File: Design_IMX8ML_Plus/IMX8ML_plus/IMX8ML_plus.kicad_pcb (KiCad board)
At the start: 6 copper layers, 50 x 80 mm, 167 parts, among them J1 DF40C-100DP-0.4V_51_, J2 DF40C-100DP-0.4V_51_, J3 DF40C-100DP-0.4V_51_, J4 DF40C-100DP-0.4V_51_, U1 MIMX8ML8CVNKZAB, U2 MT53E1536M32D4DT-046 WT:A, U3 SDINBDG4-8G, U4 PCA9450CHNY, U5 MT25QUxxxxxx1xW7, U6 KSZ9131RNXI, Y1 32.768KHz, Y2 24MHz, Y3 32.768KHz

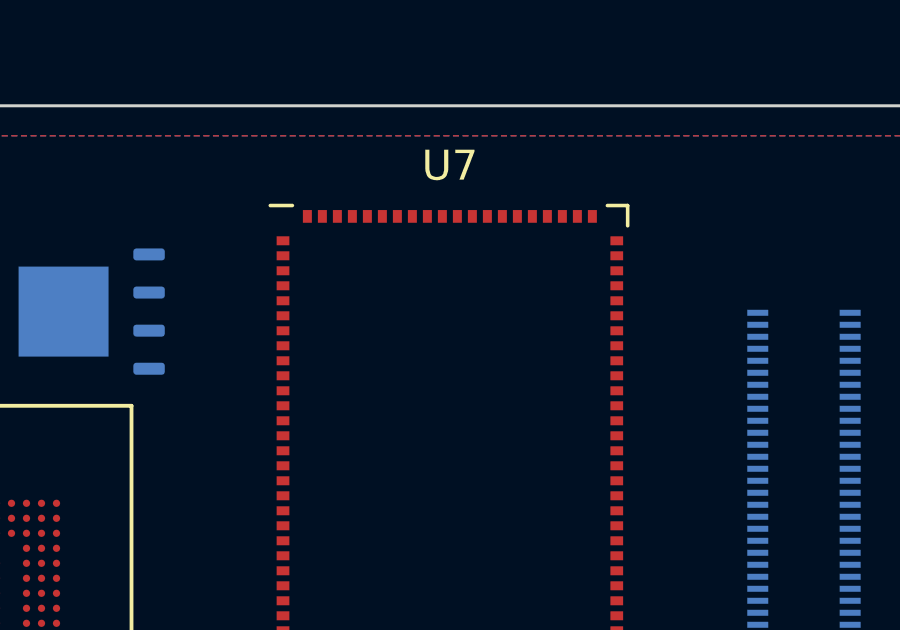
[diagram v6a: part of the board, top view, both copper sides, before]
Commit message: reorganization of the componentes
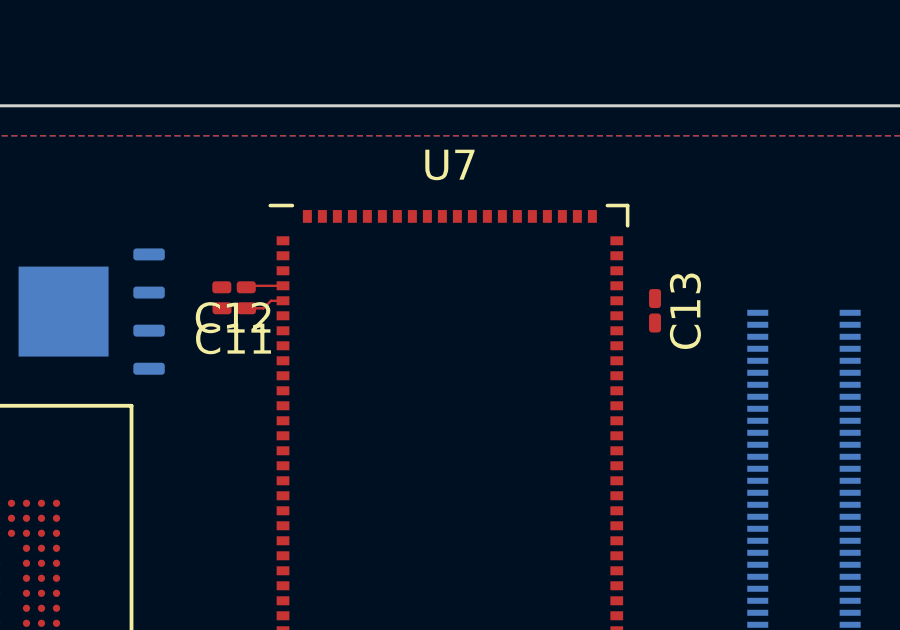
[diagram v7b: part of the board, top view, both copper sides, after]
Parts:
- added C11: 100nF, Capacitor_SMD:C_0201_0603Metric_Pad0.64x0.40mm_HandSolder, F.Cu at (134.8, 63.8)
- added C12: 100nF, Capacitor_SMD:C_0201_0603Metric_Pad0.64x0.40mm_HandSolder, F.Cu at (134.7, 63.0)
- added C13: 100nF, Capacitor_SMD:C_0201_0603Metric_Pad0.64x0.40mm_HandSolder, F.Cu at (148.8, 63.8)
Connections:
- U7 pad 17: Net-(U7-GND-Pad17) -> GND
- U7 pad 20: Net-(U7-GND-Pad17) -> GND
- U7 pad 23: Net-(U7-GND-Pad17) -> GND
- U7 pad 26: Net-(U7-GND-Pad17) -> GND
- U7 pad 32: Net-(U7-GND-Pad17) -> GND
- U7 pad 35: Net-(U7-GND-Pad32) -> GND
- U7 pad 38: Net-(U7-GND-Pad32) -> GND
- U7 pad 4: unconnected-(U7-VDD33-Pad4) -> +3V3
- U7 pad 41: Net-(U7-GND-Pad32) -> GND
- U7 pad 5: unconnected-(U7-VDD33-Pad5) -> +3V3
- U7 pad 6: Net-(U7-GND-Pad17) -> GND
- U7 pad 62: Net-(U7-GND-Pad17) -> GND
- U7 pad 68: Net-(U7-GND-Pad17) -> GND
- U7 pad 71: Net-(U7-GND-Pad17) -> GND
- U7 pad 72: unconnected-(U7-VD33-Pad72) -> +3V3
- U7 pad 74: Net-(U7-GND-Pad17) -> GND
- U7 pad 75: Net-(U7-GND-Pad17) -> GND
- U7 pad 76: Net-(U7-GND-Pad17) -> GND
- U7 pad 77: Net-(U7-GND-Pad17) -> GND
- U7 pad 78: Net-(U7-GND-Pad17) -> GND
- U7 pad 79: Net-(U7-GND-Pad17) -> GND
- U7 pad 80: Net-(U7-GND-Pad17) -> GND
- U7 pad 81: Net-(U7-GND-Pad17) -> GND
- U7 pad 82: Net-(U7-GND-Pad17) -> GND
- U7 pad 83: Net-(U7-GND-Pad17) -> GND
- U7 pad 84: Net-(U7-GND-Pad17) -> GND
- U7 pad 85: Net-(U7-GND-Pad17) -> GND
- U7 pad 86: Net-(U7-GND-Pad17) -> GND
- U7 pad 87: Net-(U7-GND-Pad17) -> GND
- U7 pad 89: Net-(U7-GND-Pad17) -> GND
- U7 pad 90: Net-(U7-GND-Pad17) -> GND
- U7 pad 91: Net-(U7-GND-Pad17) -> GND
- U7 pad 92: Net-(U7-GND-Pad17) -> GND
- U7 pad 93: Net-(U7-GND-Pad17) -> GND
- U7 pad 94: Net-(U7-GND-Pad17) -> GND
- U7 pad 95: Net-(U7-GND-Pad17) -> GND
- U7 pad 96: Net-(U7-GND-Pad17) -> GND
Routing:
- net +3V3: track 0.00 -> 2.57 mm
